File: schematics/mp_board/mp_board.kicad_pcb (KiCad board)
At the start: 4 copper layers, 45.5 x 46 mm, 50 parts, among them J1 i2c_1, J10 swd, J12 pins_e, J13 pins_f, J2 i2c_2, J3 boot_rst, J4 pins_b, J5 pins_a, J6 MY_USB_B, J7 pins_c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

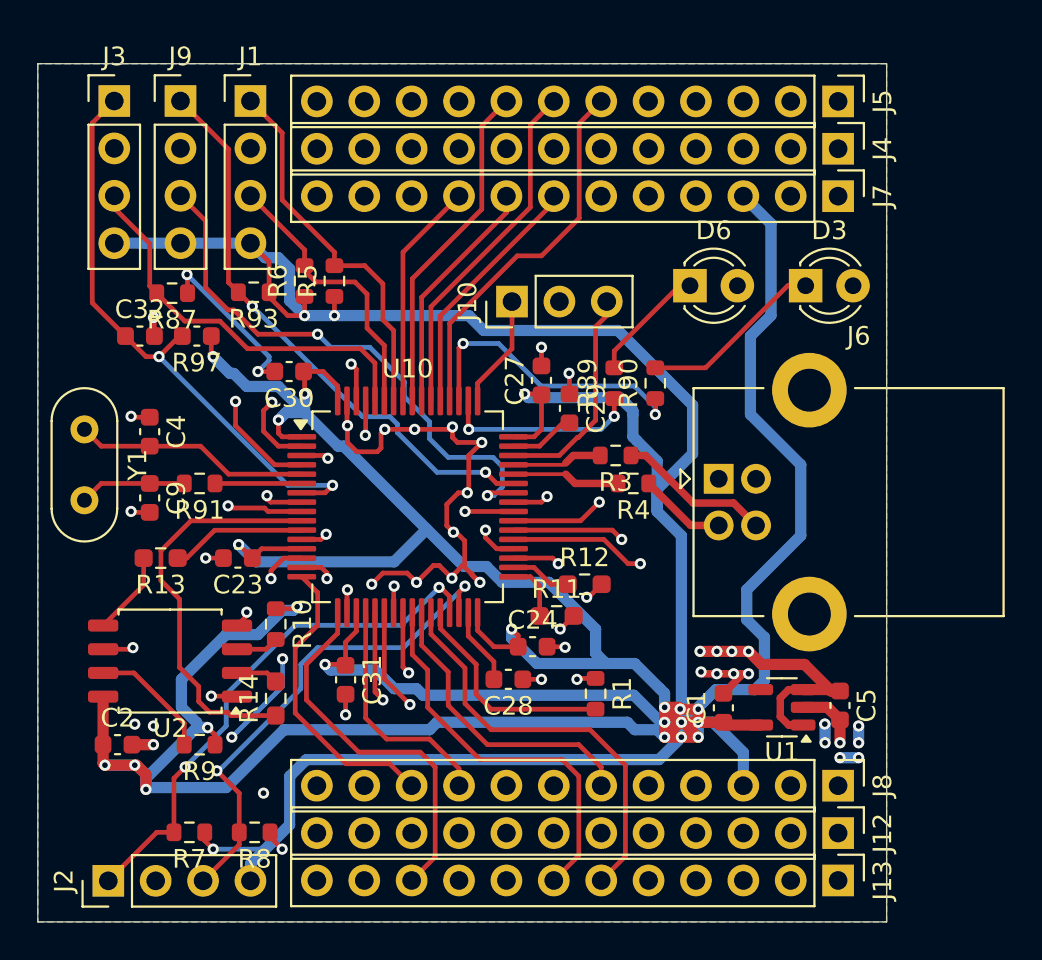
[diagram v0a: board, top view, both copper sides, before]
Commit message: Moved wires and created a few more gnd vias.
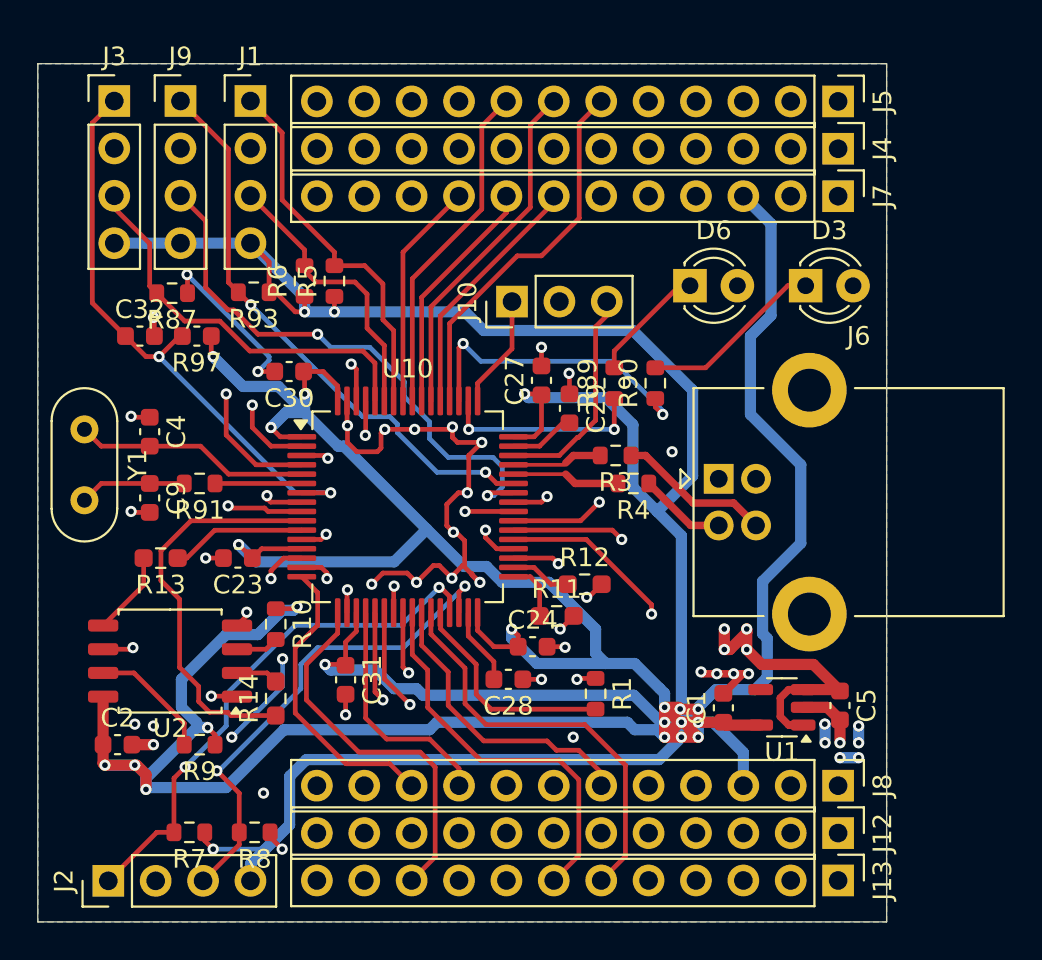
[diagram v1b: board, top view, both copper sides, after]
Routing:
- net GND: track 320.7 -> 346.8 mm, vias 43 -> 45
- net /Vbus: track 81.8 -> 84.2 mm
- net VDD: track 335.2 -> 333.8 mm
- net /pc15: track 24.9 -> 25.9 mm
- net /pc6: track 27.9 -> 26.9 mm
- net /pc14: track 21.2 -> 22.1 mm
- net /pc13: track 24.0 -> 24.7 mm
